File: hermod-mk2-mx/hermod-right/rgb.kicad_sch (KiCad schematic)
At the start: 84 parts

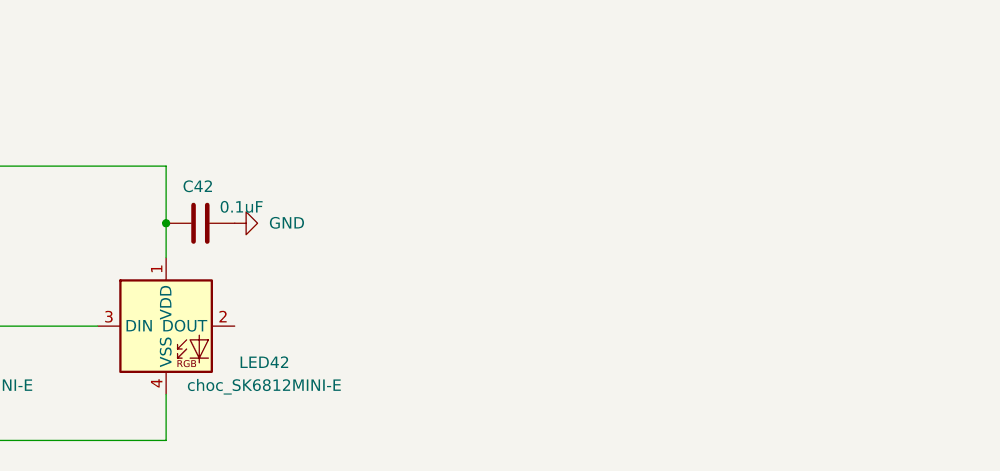
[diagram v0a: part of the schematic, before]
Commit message: Added switches to hermod 3 and updated mist thumb spacing
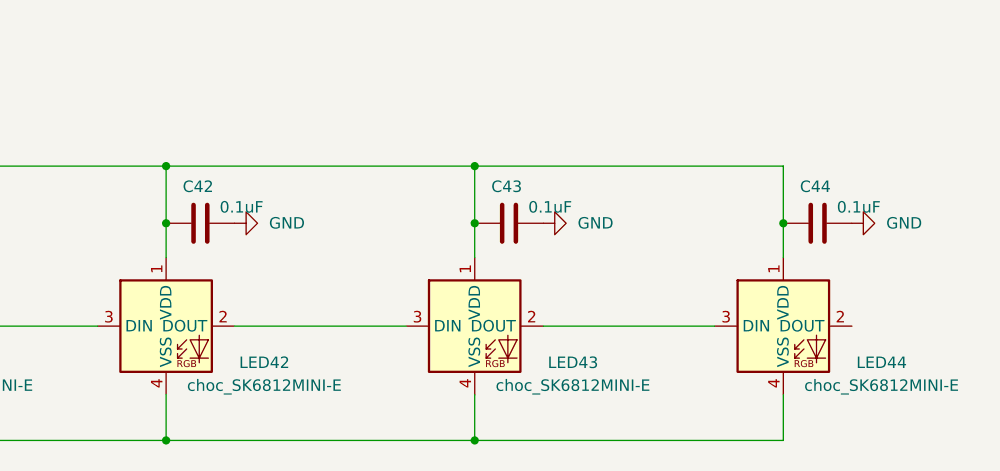
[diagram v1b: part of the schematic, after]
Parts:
- added C43, C44: 0.1uF, Capacitor_SMD:C_0402_1005Metric, symbol Device:C
- added LED43, LED44: choc_SK6812MINI-E, PCM_marbastlib-choc:LED_choc_6028R, symbol PCM_marbastlib-choc:choc_SK6812MINI-E
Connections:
- net +5V: now also C43.1, C44.1, LED43.1 (VDD), LED44.1 (VDD)
- net GND: now also C43.2, C44.2, LED43.4 (VSS), LED44.4 (VSS)
- net at LED42.2 (DOUT): now also LED43.3 (DIN)
- new net: LED43.2 (DOUT), LED44.3 (DIN)
